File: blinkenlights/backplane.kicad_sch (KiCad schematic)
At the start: 18 parts, among them J201 Conn_03x32_Row_Letter_First, J202 Conn_02x20_Odd_Even, J203 Conn_02x20_Odd_Even, J204 Conn_02x20_Odd_Even, J205 Conn_02x20_Odd_Even

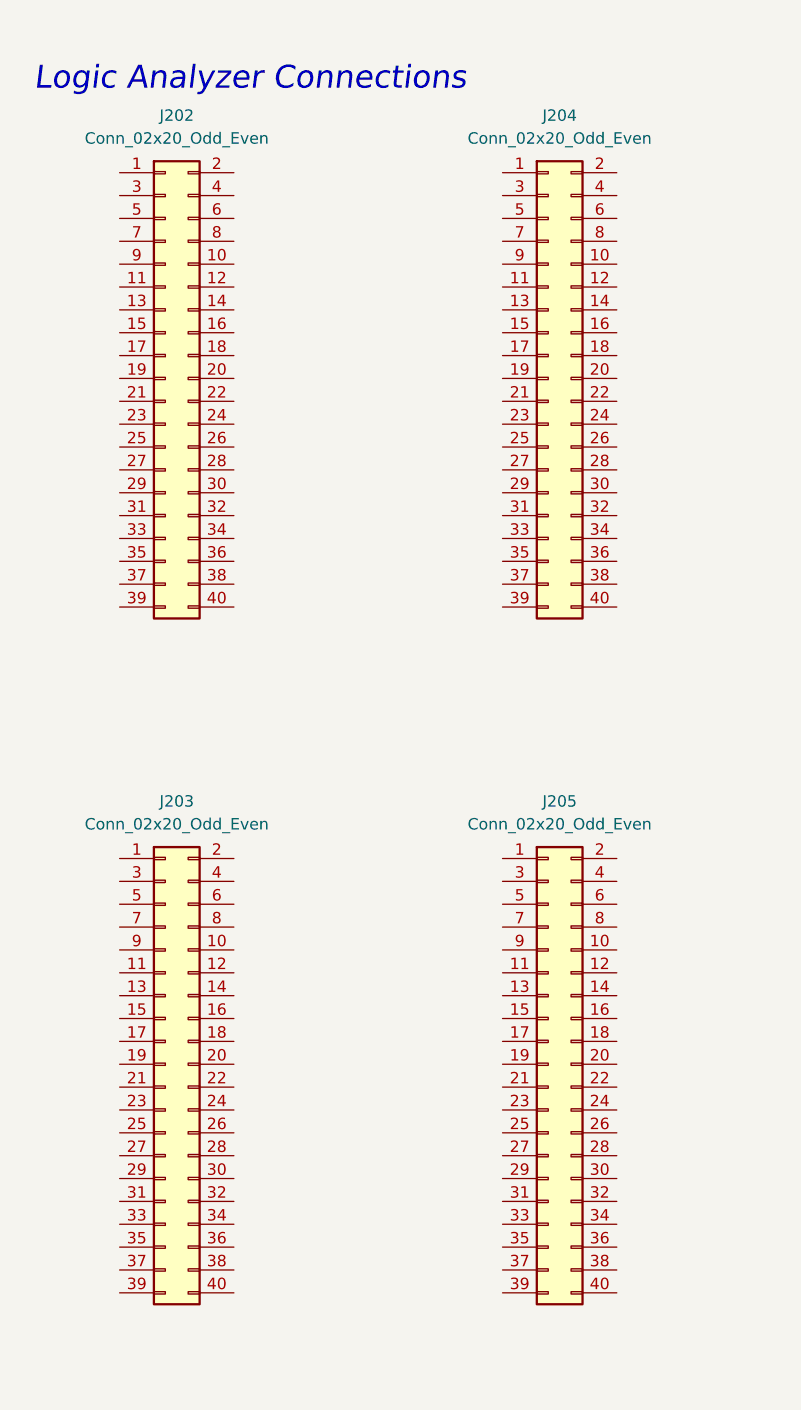
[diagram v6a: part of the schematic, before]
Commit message: Added Teensy, logic probe ports to blinkenlights
- A teensy 4.0 is on board connected to the IO expanders (and directly,
  the /HALT line, so it can single step the CPU on request) rather than
  expecting an external connection.

- Routed all bus signals to the logic analyzer connectors. They're meant
  to connect to a 16700-series pod connector on a 0.1" spacing, with 16
  signal lines, and one clock (CLK) with all other pins tied to ground.
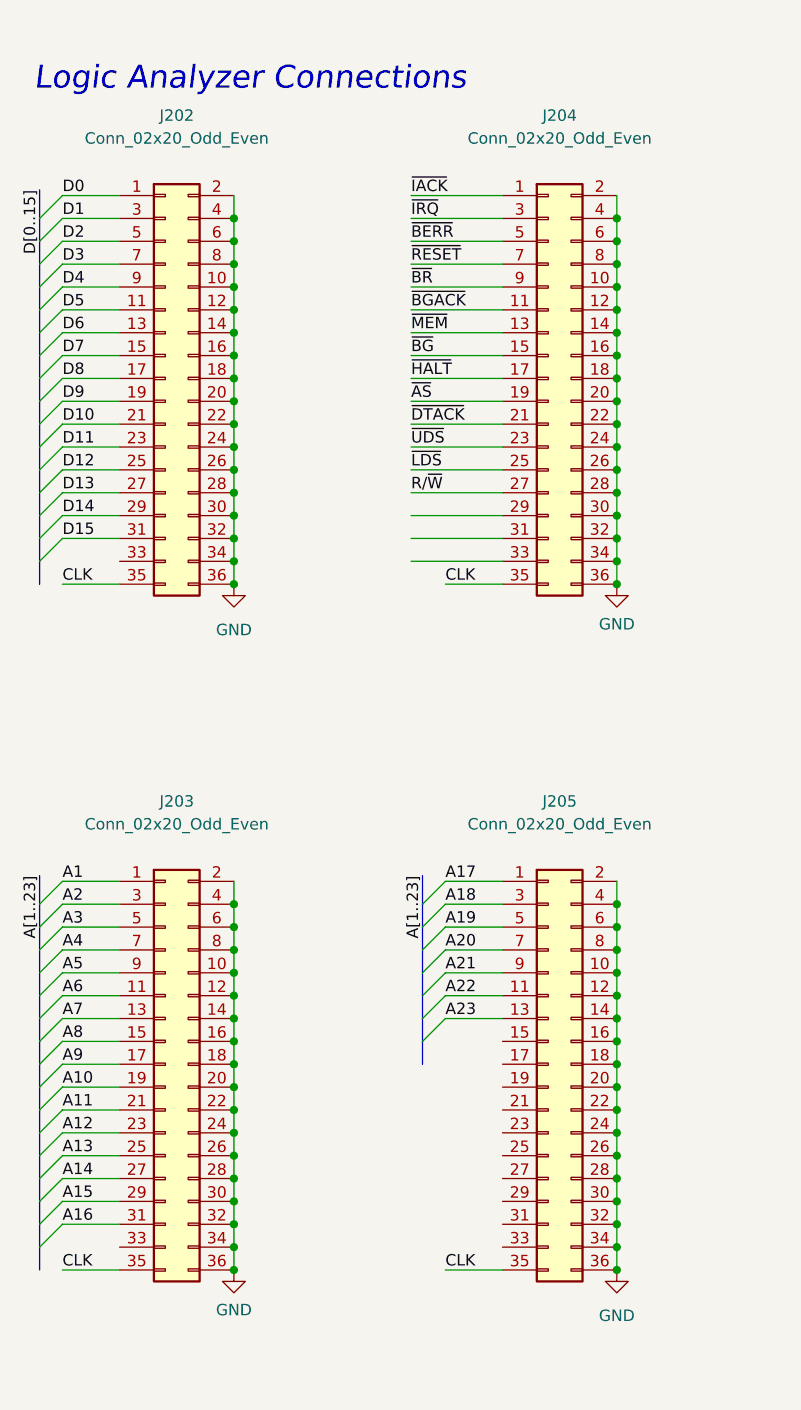
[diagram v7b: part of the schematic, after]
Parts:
- J202, J203, J204, J205: footprint Connector_PinHeader_2.54mm:PinHeader_2x20_P2.54mm_Vertical -> Connector_PinHeader_2.54mm:PinHeader_2x18_P2.54mm_Vertical; symbol Connector_Generic:Conn_02x20_Odd_Even -> Connector_Generic:Conn_02x18_Odd_Even
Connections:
- net A1: now also J203.1 (Pin_1)
- net A10: now also J203.19 (Pin_19)
- net A11: now also J203.21 (Pin_21)
- net A12: now also J203.23 (Pin_23)
- net A13: now also J203.25 (Pin_25)
- net A14: now also J203.27 (Pin_27)
- net A15: now also J203.29 (Pin_29)
- net A16: now also J203.31 (Pin_31)
- net A17: now also J205.1 (Pin_1)
- net A18: now also J205.3 (Pin_3)
- net A19: now also J205.5 (Pin_5)
- net A2: now also J203.3 (Pin_3)
- net A20: now also J205.7 (Pin_7)
- net A21: now also J205.9 (Pin_9)
- net A22: now also J205.11 (Pin_11)
- net A23: now also J205.13 (Pin_13)
- net A3: now also J203.5 (Pin_5)
- net A4: now also J203.7 (Pin_7)
- net A5: now also J203.9 (Pin_9)
- net A6: now also J203.11 (Pin_11)
- net A7: now also J203.13 (Pin_13)
- net A8: now also J203.15 (Pin_15)
- net A9: now also J203.17 (Pin_17)
- net CLK: now also J202.35 (Pin_35), J203.35 (Pin_35), J204.35 (Pin_35), J205.35 (Pin_35)
- net D0: now also J202.1 (Pin_1)
- net D1: now also J202.3 (Pin_3)
- net D10: now also J202.21 (Pin_21)
- net D11: now also J202.23 (Pin_23)
- net D12: now also J202.25 (Pin_25)
- net D13: now also J202.27 (Pin_27)
- net D14: now also J202.29 (Pin_29)
- net D15: now also J202.31 (Pin_31)
- net D2: now also J202.5 (Pin_5)
- net D3: now also J202.7 (Pin_7)
- net D4: now also J202.9 (Pin_9)
- net D5: now also J202.11 (Pin_11)
- net D6: now also J202.13 (Pin_13)
- net D7: now also J202.15 (Pin_15)
- net D8: now also J202.17 (Pin_17)
- net D9: now also J202.19 (Pin_19)
- net GND: now also J202.10 (Pin_10), J202.12 (Pin_12), J202.14 (Pin_14), J202.16 (Pin_16), J202.18 (Pin_18), J202.2 (Pin_2), J202.20 (Pin_20), J202.22 (Pin_22), J202.24 (Pin_24), J202.26 (Pin_26), J202.28 (Pin_28), J202.30 (Pin_30), J202.32 (Pin_32), J202.34 (Pin_34), J202.36 (Pin_36), J202.4 (Pin_4), J202.6 (Pin_6), J202.8 (Pin_8), J203.10 (Pin_10), J203.12 (Pin_12), J203.14 (Pin_14), J203.16 (Pin_16), J203.18 (Pin_18), J203.2 (Pin_2), J203.20 (Pin_20), J203.22 (Pin_22), J203.24 (Pin_24), J203.26 (Pin_26), J203.28 (Pin_28), J203.30 (Pin_30), J203.32 (Pin_32), J203.34 (Pin_34), J203.36 (Pin_36), J203.4 (Pin_4), J203.6 (Pin_6), J203.8 (Pin_8), J204.10 (Pin_10), J204.12 (Pin_12), J204.14 (Pin_14), J204.16 (Pin_16), J204.18 (Pin_18), J204.2 (Pin_2), J204.20 (Pin_20), J204.22 (Pin_22), J204.24 (Pin_24), J204.26 (Pin_26), J204.28 (Pin_28), J204.30 (Pin_30), J204.32 (Pin_32), J204.34 (Pin_34), J204.36 (Pin_36), J204.4 (Pin_4), J204.6 (Pin_6), J204.8 (Pin_8), J205.10 (Pin_10), J205.12 (Pin_12), J205.14 (Pin_14), J205.16 (Pin_16), J205.18 (Pin_18), J205.2 (Pin_2), J205.20 (Pin_20), J205.22 (Pin_22), J205.24 (Pin_24), J205.26 (Pin_26), J205.28 (Pin_28), J205.30 (Pin_30), J205.32 (Pin_32), J205.34 (Pin_34), J205.36 (Pin_36), J205.4 (Pin_4), J205.6 (Pin_6), J205.8 (Pin_8)
- net R/~{W}: now also J204.27 (Pin_27)
- net ~{AS}: now also J204.19 (Pin_19)
- net ~{BERR}: now also J204.5 (Pin_5)
- net ~{BGACK}: now also J204.11 (Pin_11)
- net ~{BG}: now also J204.15 (Pin_15)
- net ~{BR}: now also J204.9 (Pin_9)
- net ~{DTACK}: now also J204.21 (Pin_21)
- net ~{HALT}: now also J204.17 (Pin_17)
- net ~{IACK}: now also J204.1 (Pin_1)
- net ~{IRQ}: now also J204.3 (Pin_3)
- net ~{LDS}: now also J204.25 (Pin_25)
- net ~{MEM}: now also J204.13 (Pin_13)
- net ~{RESET}: now also J204.7 (Pin_7)
- net ~{UDS}: now also J204.23 (Pin_23)

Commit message: Finish routing of blinkenlights board
- Completed routing of the board, including the function code lines and
  other such fun stuff
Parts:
- added U201: AT24CS32-SSHM, Package_SO:SOIC-8_3.9x4.9mm_P1.27mm, symbol Memory_EEPROM:AT24CS32-SSHM
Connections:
- net +5V: now also U201.1 (A0), U201.2 (A1), U201.3 (A2), U201.8 (VCC)
- net GND: now also U201.4 (GND), U201.7 (WP)
- net I2C_SCL: now also U201.6 (SCL)
- net I2C_SDA: now also U201.5 (SDA)
- net FC1: now reaches J201.a25 (Pin_a25)
- net FC1: now also J205.17 (Pin_17)
- net FC0: now reaches J201.b25 (Pin_b25)
- net FC0: now also J205.19 (Pin_19)
- net FC2: now reaches J201.c25 (Pin_c25)
- net FC2: now also J205.21 (Pin_21)
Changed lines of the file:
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@@
   (junction (at 86.995 113.03) (diameter 0) (color 0 0 0 0)
   )
+  (junction (at 132.715 177.8) (diameter 0) (color 0 0 0 0)
+  )
   (junction (at 207.01 158.75) (diameter 0) (color 0 0 0 0)
   )
@@
   (junction (at 86.995 128.27) (diameter 0) (color 0 0 0 0)
   )
+  (junction (at 132.715 180.34) (diameter 0) (color 0 0 0 0)
+  )
   (junction (at 224.155 95.25) (diameter 0) (color 0 0 0 0)
   )
@@
     (stroke (width 0) (type default) (color 0 0 0 0))
   )
+  (wire (pts (xy 224.155 80.01) (xy 225.425 80.01))
+    (stroke (width 0) (type default) (color 0 0 0 0))
+  )
   (bus (pts (xy 65.405 107.315) (xy 65.405 110.49))
     (stroke (width 0) (type default) (color 0 0 0 0))
@@
     (stroke (width 0) (type default) (color 0 0 0 0))
   )
+  (wire (pts (xy 259.08 80.01) (xy 260.35 80.01))
+    (stroke (width 0) (type default) (color 0 0 0 0))
+  )
   (wire (pts (xy 44.45 133.35) (xy 44.45 135.89))
     (stroke (width 0) (type default) (color 0 0 0 0))
   )
+  (wire (pts (xy 64.135 133.35) (xy 74.295 133.35))
+    (stroke (width 0) (type default) (color 0 0 0 0))
+  )
   (bus (pts (xy 202.565 46.99) (xy 202.565 52.07))
     (stroke (width 0) (type default) (color 0 0 0 0))
@@
     (stroke (width 0) (type default) (color 0 0 0 0))
   )
-  (bus (pts (xy 65.405 125.73) (xy 65.405 128.27))
-    (stroke (width 0) (type default) (color 0 0 0 0))
-  )
   (wire (pts (xy 260.35 87.63) (xy 254 87.63))
     (stroke (width 0) (type default) (color 0 0 0 0))
@@
     (stroke (width 0) (type default) (color 0 0 0 0))
   )
+  (wire (pts (xy 132.715 180.34) (xy 132.715 182.88))
+    (stroke (width 0) (type default) (color 0 0 0 0))
+  )
   (bus (pts (xy 65.405 113.03) (xy 65.405 115.57))
     (stroke (width 0) (type default) (color 0 0 0 0))
@@
     (stroke (width 0) (type default) (color 0 0 0 0))
   )
+  (wire (pts (xy 153.035 177.8) (xy 165.1 177.8))
+    (stroke (width 0) (type default) (color 0 0 0 0))
+  )
   (bus (pts (xy 22.86 31.115) (xy 22.86 34.29))
     (stroke (width 0) (type default) (color 0 0 0 0))
@@
     (stroke (width 0) (type default) (color 0 0 0 0))
   )
+  (wire (pts (xy 64.135 130.81) (xy 74.295 130.81))
+    (stroke (width 0) (type default) (color 0 0 0 0))
+  )
   (wire (pts (xy 25.4 133.35) (xy 31.75 133.35))
     (stroke (width 0) (type default) (color 0 0 0 0))
@@
     (stroke (width 0) (type default) (color 0 0 0 0))
   )
+  (wire (pts (xy 64.135 128.27) (xy 74.295 128.27))
+    (stroke (width 0) (type default) (color 0 0 0 0))
+  )
   (wire (pts (xy 44.45 57.15) (xy 44.45 59.69))
     (stroke (width 0) (type default) (color 0 0 0 0))
@@
     (stroke (width 0) (type default) (color 0 0 0 0))
   )
+  (wire (pts (xy 153.035 180.34) (xy 165.1 180.34))
+    (stroke (width 0) (type default) (color 0 0 0 0))
+  )
   (wire (pts (xy 44.45 118.11) (xy 44.45 120.65))
     (stroke (width 0) (type default) (color 0 0 0 0))
@@
     (stroke (width 0) (type default) (color 0 0 0 0))
   )
+  (wire (pts (xy 210.185 80.01) (xy 211.455 80.01))
+    (stroke (width 0) (type default) (color 0 0 0 0))
+  )
   (wire (pts (xy 210.185 77.47) (xy 211.455 77.47))
     (stroke (width 0) (type default) (color 0 0 0 0))
@@
   )
   (wire (pts (xy 67.945 110.49) (xy 74.295 110.49))
+    (stroke (width 0) (type default) (color 0 0 0 0))
+  )
+  (wire (pts (xy 132.715 177.8) (xy 132.715 180.34))
     (stroke (width 0) (type default) (color 0 0 0 0))
   )
@@
     (effects (font (size 1.27 1.27)) (justify left bottom))
   )
+  (label "I2C_SDA" (at 165.1 177.8 180)
+    (effects (font (size 1.27 1.27)) (justify right bottom))
+  )
   (label "A[1..23]" (at 202.565 44.45 270)
     (effects (font (size 1.27 1.27)) (justify right bottom))
@@
     (effects (font (size 1.27 1.27)) (justify left bottom))
   )
+  (label "FC0" (at 64.135 130.81 0)
+    (effects (font (size 1.27 1.27)) (justify left bottom))
+  )
   (label "~{BG}" (at 64.135 49.53 0)
     (effects (font (size 1.27 1.27)) (justify left bottom))
@@
     (effects (font (size 1.27 1.27)) (justify left bottom))
   )
+  (label "FC1" (at 64.135 128.27 0)
+    (effects (font (size 1.27 1.27)) (justify left bottom))
+  )
   (label "D6" (at 25.4 46.99 0)
     (effects (font (size 1.27 1.27)) (justify left bottom))
@@
     (effects (font (size 1.27 1.27)) (justify left bottom))
   )
+  (label "I2C_SCL" (at 165.1 180.34 180)
+    (effects (font (size 1.27 1.27)) (justify right bottom))
+  )
   (label "A23" (at 67.945 123.19 0)
     (effects (font (size 1.27 1.27)) (justify left bottom))
@@
   )
   (label "D0" (at 25.4 31.75 0)
+    (effects (font (size 1.27 1.27)) (justify left bottom))
+  )
+  (label "FC2" (at 64.135 133.35 0)
     (effects (font (size 1.27 1.27)) (justify left bottom))
   )
@@
     (effects (font (size 1.27 1.27)) (justify left))
   )
+  (hierarchical_label "FC[0..2]" (shape bidirectional) (at 170.815 74.295 0)
+    (effects (font (size 1.27 1.27)) (justify left))
+  )
   (hierarchical_label "I2C_SDA" (shape tri_state) (at 254 24.13 180)
     (effects (font (size 1.27 1.27)) (justify right))
@@
     (effects (font (size 1.27 1.27)) (justify left))
   )
+  (hierarchical_label "FC2" (shape bidirectional) (at 259.08 80.01 180)
+    (effects (font (size 1.27 1.27)) (justify right))
+  )
   (hierarchical_label "A[1..23]" (shape bidirectional) (at 251.46 69.85 270)
     (effects (font (size 1.27 1.27)) (justify right))
@@
   (hierarchical_label "~{IRQ}" (shape input) (at 230.505 92.71 0)
     (effects (font (size 1.27 1.27)) (justify left))
+  )
+  (hierarchical_label "FC0" (shape bidirectional) (at 225.425 80.01 0)
+    (effects (font (size 1.27 1.27)) (justify left))
+  )
+  (hierarchical_label "FC1" (shape bidirectional) (at 210.185 80.01 180)
+    (effects (font (size 1.27 1.27)) (justify right))
   )
   (hierarchical_label "~{UDS}" (shape bidirectional) (at 254 72.39 180)
@@
     (pin "1")
     (pin "2")
+  )
+  (symbol (lib_id "Memory_EEPROM:AT24CS32-SSHM") (at 142.875 180.34 0) (unit 1)
+    (in_bom yes) (on_board yes)
+    (property "Reference" "U201" (id 0) (at 142.875 163.83 0))
+    (property "Value" "AT24CS32-SSHM" (id 1) (at 142.875 166.6051 0))
+    (property "Footprint" "Package_SO:SOIC-8_3.9x4.9mm_P1.27mm" (id 2) (at 142.875 180.34 0)
+      (effects (font (size 1.27 1.27)) hide)
+    )
+    (property "Datasheet" "http://ww1.microchip.com/downloads/en/DeviceDoc/Atmel-8869-SEEPROM-AT24CS32-Datasheet.pdf" (id 3) (at 142.875 180.34 0)
+      (effects (font (size 1.27 1.27)) hide)
+    )
+    (property "MPN" "AT24CS32-SSHM-T" (id 4) (at 142.875 180.34 0)
+      (effects (font (size 1.27 1.27)) hide)
+    )
+    (pin "1")
+    (pin "2")
+    (pin "3")
+    (pin "4")
+    (pin "5")
+    (pin "6")
+    (pin "7")
+    (pin "8")
   )
   (symbol (lib_id "power:GND") (at 260.35 44.45 270) (unit 1)
@@
     (pin "2")
   )
+  (symbol (lib_id "power:GND") (at 142.875 187.96 0) (unit 1)
+    (in_bom yes) (on_board yes) (fields_autoplaced)
+    (property "Reference" "#PWR0229" (id 0) (at 142.875 194.31 0)
+      (effects (font (size 1.27 1.27)) hide)
+    )
+    (property "Value" "GND" (id 1) (at 142.875 193.04 0))
+    (property "Footprint" "" (id 2) (at 142.875 187.96 0)
+      (effects (font (size 1.27 1.27)) hide)
+    )
+    (property "Datasheet" "" (id 3) (at 142.875 187.96 0)
+      (effects (font (size 1.27 1.27)) hide)
+    )
+    (pin "1")
+  )
   (symbol (lib_id "power:GND") (at 224.155 39.37 90) (unit 1)
     (in_bom yes) (on_board yes) (fields_autoplaced)
@@
     (pin "1")
   )
+  (symbol (lib_id "power:GND") (at 153.035 182.88 0) (unit 1)
+    (in_bom yes) (on_board yes) (fields_autoplaced)
+    (property "Reference" "#PWR?" (id 0) (at 153.035 189.23 0)
+      (effects (font (size 1.27 1.27)) hide)
+    )
+    (property "Value" "GND" (id 1) (at 153.035 187.96 0))
+    (property "Footprint" "" (id 2) (at 153.035 182.88 0)
+      (effects (font (size 1.27 1.27)) hide)
+    )
+    (property "Datasheet" "" (id 3) (at 153.035 182.88 0)
+      (effects (font (size 1.27 1.27)) hide)
+    )
+    (pin "1")
+  )
   (symbol (lib_id "Connector:TestPoint") (at 264.795 111.76 270) (unit 1)
     (in_bom yes) (on_board yes)
@@
     )
     (property "Datasheet" "" (id 3) (at 260.35 95.25 0)
+      (effects (font (size 1.27 1.27)) hide)
+    )
+    (pin "1")
+  )
+  (symbol (lib_id "power:+5V") (at 132.715 177.8 90) (unit 1)
+    (in_bom yes) (on_board yes) (fields_autoplaced)
+    (property "Reference" "#PWR0227" (id 0) (at 136.525 177.8 0)
+      (effects (font (size 1.27 1.27)) hide)
+    )
+    (property "Value" "+5V" (id 1) (at 129.54 178.279 90)
+      (effects (font (size 1.27 1.27)) (justify left))
+    )
+    (property "Footprint" "" (id 2) (at 132.715 177.8 0)
+      (effects (font (size 1.27 1.27)) hide)
+    )
+    (property "Datasheet" "" (id 3) (at 132.715 177.8 0)
       (effects (font (size 1.27 1.27)) hide)
     )
@@
       (effects (font (size 1.27 1.27)) hide)
     )
+    (pin "1")
+  )
+  (symbol (lib_id "power:+5V") (at 142.875 172.72 0) (unit 1)
+    (in_bom yes) (on_board yes)
+    (property "Reference" "#PWR0228" (id 0) (at 142.875 176.53 0)
+      (effects (font (size 1.27 1.27)) hide)
+    )
+    (property "Value" "+5V" (id 1) (at 142.875 168.91 0))
+    (property "Footprint" "" (id 2) (at 142.875 172.72 0)
+      (effects (font (size 1.27 1.27)) hide)
+    )
+    (property "Datasheet" "" (id 3) (at 142.875 172.72 0)
+      (effects (font (size 1.27 1.27)) hide)
+    )
